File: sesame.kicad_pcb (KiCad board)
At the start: 2 copper layers, 344.4 x 130.9 mm, 166 parts, among them U1 ATmega32A-PU

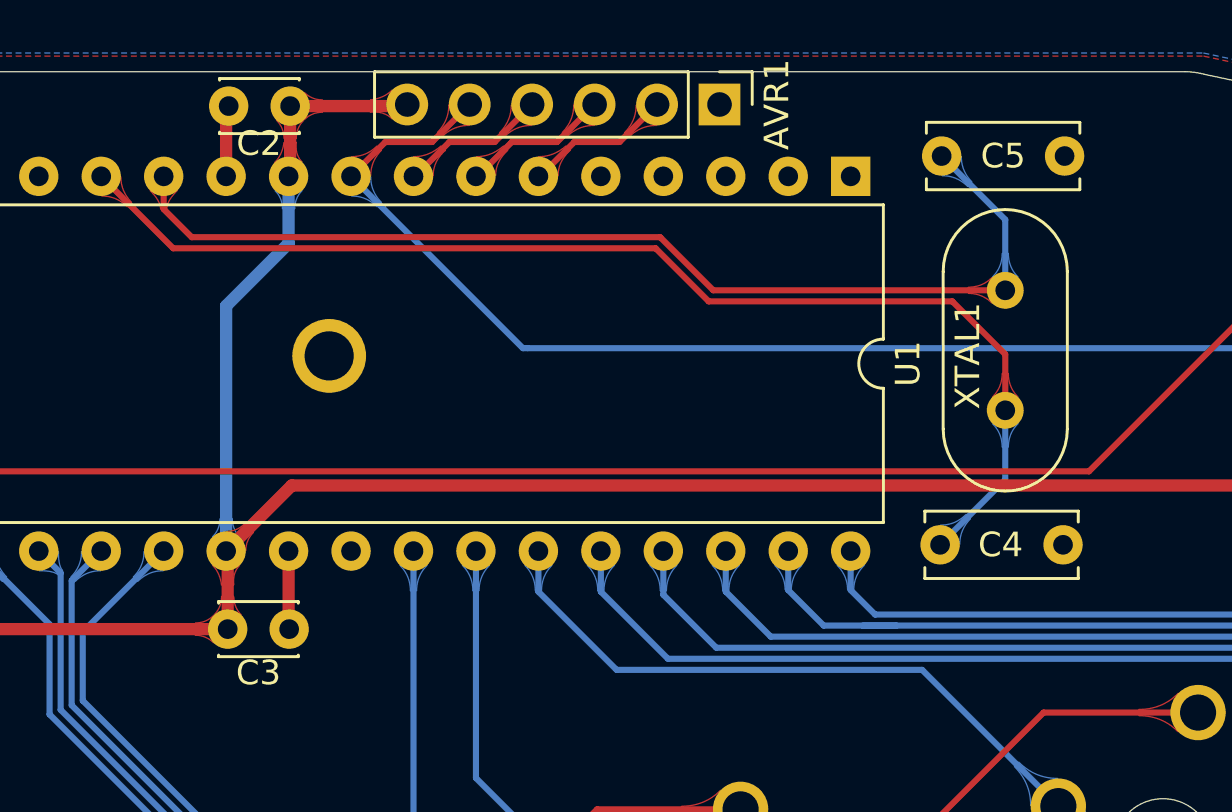
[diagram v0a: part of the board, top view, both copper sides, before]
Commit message: Use components more in line with other similar kits (Mysterium etc.)
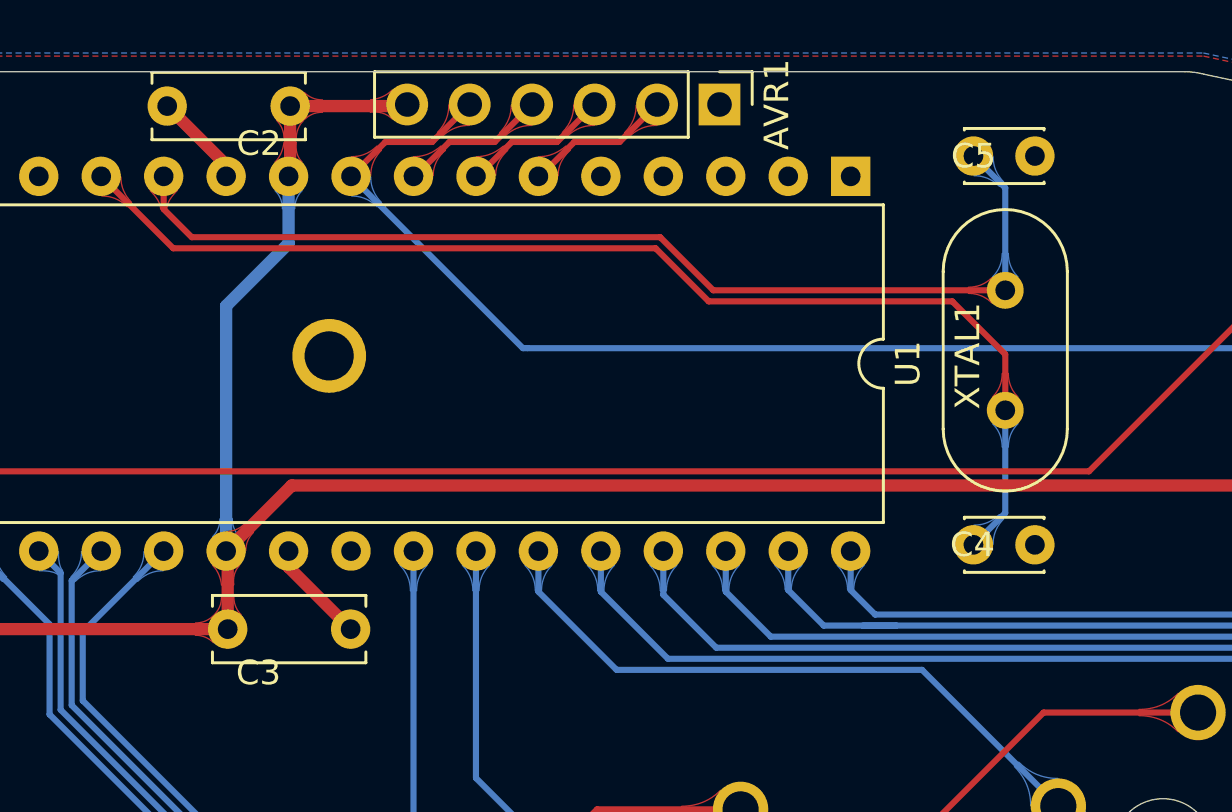
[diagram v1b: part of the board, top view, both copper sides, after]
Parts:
- C2, C3: footprint Capacitor_THT:C_Disc_D3.0mm_W2.0mm_P2.50mm -> Capacitor_THT:C_Disc_D6.0mm_W2.5mm_P5.00mm
- C4, C5: footprint Capacitor_THT:C_Disc_D6.0mm_W2.5mm_P5.00mm -> Capacitor_THT:C_Disc_D3.0mm_W2.0mm_P2.50mm
- moved C5 1.21 mm to (240.5, 69.0)
- moved C4 1.14 mm to (240.5, 84.8)
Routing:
- net GND: track 11.5 -> 13.5 mm
- net Net-(C4-Pad2): track 49.1 -> 48.5 mm
- net Net-(C5-Pad2): track 43.5 -> 42.9 mm
